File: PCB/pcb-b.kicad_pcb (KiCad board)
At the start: 2 copper layers, 116.9 x 83.4 mm, 104 parts, among them IC2 BDX34C, IC3 BDX34C, K1 RT42xxxx, Q1 D45VH10, Q10 BC337, Q11 BC337, Q12 BC327, Q13 BC337, Q14 D45VH10, Q15 D45VH10, Q16 BC337, Q17 BC337, Q18 BC327, Q19 BC327, Q2 D45VH10, Q20 BC327, Q3 BC337, Q4 BC337, Q5 BC337, Q6 BC337, Q7 BC337, Q8 BC337, Q9 BC337, U1 L7805, U2 L7805, U3 L7805, U4 ATmega16L-8P

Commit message: fixes
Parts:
- removed Bike_stand1, Decomp_1, LightOnOff_sw1, addLights1, powerOFF1: Conn_01x02, Connector_PinSocket_2.54mm:PinSocket_1x02_P2.54mm_Vertical
- removed C2: 100nF, Capacitor_THT:C_Disc_D4.3mm_W1.9mm_P5.00mm
- removed D3, D4: 2V, Diode_THT:D_DO-35_SOD27_P7.62mm_Horizontal
- removed KeyLocker1, RearDevs1: Conn_01x08, Connector_PinHeader_2.54mm:PinHeader_1x08_P2.54mm_Vertical
- removed Q19, Q20: BC327, Package_TO_SOT_THT:TO-92L_Inline_Wide
- removed R1: 1K, Resistor_THT:R_Axial_DIN0207_L6.3mm_D2.5mm_P10.16mm_Horizontal
- removed RA45: 10K, Resistor_THT:R_Axial_DIN0207_L6.3mm_D2.5mm_P7.62mm_Horizontal
- removed RA46, RA47: 3K, Resistor_THT:R_Axial_DIN0207_L6.3mm_D2.5mm_P7.62mm_Horizontal
- removed RA48, RA49: 100K, Resistor_THT:R_Axial_DIN0207_L6.3mm_D2.5mm_P7.62mm_Horizontal
- removed RS232-1: Conn_01x03, Connector_Hirose:Hirose_DF63M-3P-3.96DSA_1x03_P3.96mm_Vertical
- removed RV1, RV2: 10K, Potentiometer_THT:Potentiometer_Bourns_3296W_Vertical
- removed U4: ATmega16L-8P, Package_DIP:DIP-40_W15.24mm
- removed leftCtrls-faston1: Conn_01x01, Connector_Wire:SolderWire-0.75sqmm_1x01_D1.25mm_OD2.3mm
- removed leftCtrls_conn1, rightCtrls_conn1: Conn_01x06, Connector_PinHeader_2.54mm:PinHeader_1x06_P2.54mm_Vertical
- added to_pcA2: Conn_01x05, Connector_PinSocket_2.54mm:PinSocket_1x05_P2.54mm_Vertical, F.Cu at (135.1, 112.2)
- added to_pcA3: Conn_01x05, Connector_PinSocket_2.54mm:PinSocket_1x05_P2.54mm_Vertical, F.Cu at (182.8, 112.2)
- added to_pcbA1: Conn_01x06, Connector_PinSocket_2.54mm:PinSocket_1x06_P2.54mm_Vertical, F.Cu at (135.2, 86.7)
- added to_pcbA4: Conn_01x06, Connector_PinSocket_2.54mm:PinSocket_1x06_P2.54mm_Vertical, F.Cu at (182.6, 86.8)
- Q12: value BC327 -> BC337
- Q16, Q17: value BC337 -> BC327
- RA15: footprint Resistor_THT:R_Axial_DIN0207_L6.3mm_D2.5mm_P7.62mm_Horizontal -> Resistor_THT:R_Axial_DIN0414_L11.9mm_D4.5mm_P15.24mm_Horizontal
- RA23: value 5K -> 100K
- RA29: value 10K -> 1K
- RA31: value 100K -> 3K
- RA33: value 10K -> 3K
- RA41: value 4K -> 100K
- RA43, RA44: value 100K -> 10K
- RA7: value 1K -> 5K
- RA8: value 4K -> 10K
- moved K1 105.5 mm to (103.4, 135.2), turned to 0 degrees
- moved RA15 103.0 mm to (214.1, 65.9)
- moved RA42 89.9 mm to (187.0, 79.9)
- moved koso-1 77.3 mm to (202.7, 60.3), turned to 90 degrees
- moved RA29 59.3 mm to (140.7, 82.9), turned to 0 degrees
- moved Q12 58.3 mm to (142.5, 80.2), turned to 90 degrees
- moved Q16 57.2 mm to (152.7, 87.5), turned to 0 degrees
- moved Q18 53.6 mm to (177.5, 74.3), turned to 0 degrees
- moved RA7 52.2 mm to (141.0, 72.3), turned to 0 degrees
- moved RA30 51.2 mm to (165.6, 79.6)
- moved Q13 47.9 mm to (163.1, 76.1)
- moved RA31 46.8 mm to (173.2, 76.1), turned to 180 degrees
- moved Q9 46.0 mm to (136.7, 73.3), turned to -90 degrees
- moved USB-5V1 45.9 mm to (145.8, 136.5)
- moved RA34 44.8 mm to (125.2, 73.3), turned to 180 degrees
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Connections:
- K1 pad A2: +12V -> tempPower
- Q11 pad 1: Net-(Q11-Pad1) -> Net-(K1-PadA1)
- Q11 pad 2: Net-(D4-Pad2) -> Net-(Q11-Pad2)
- Q12 pad 1: tempPower -> Net-(Q12-Pad1)
- Q12 pad 2: Net-(Q12-Pad2) -> i_powerOFF
- Q12 pad 3: +5V -> GND
- Q13 pad 1: Net-(K1-PadA1) -> Net-(Q13-Pad1)
- Q13 pad 2: Net-(D3-Pad2) -> Net-(Q13-Pad2)
- Q16 pad 1: Net-(Q16-Pad1) -> tempPower
- Q16 pad 3: GND -> +5V
- Q17 pad 1: Net-(D3-Pad1) -> Net-(Q17-Pad1)
- Q17 pad 3: GND -> +12V
- Q18 pad 1: GND -> Net-(Q17-Pad1)
- Q18 pad 3: Net-(D4-Pad1) -> +12V
- RA23 pad 1: Net-(Q9-Pad2) -> Net-(Q16-Pad2)
- RA23 pad 2: o_horn -> +5V
- RA29 pad 1: Net-(Q18-Pad2) -> Net-(Q12-Pad1)
- RA29 pad 2: i_powerOFF -> Net-(Q16-Pad2)
- RA30 pad 1: Net-(D4-Pad2) -> Net-(Q13-Pad1)
- RA30 pad 2: GND -> +12V
- RA31 pad 1: Net-(D3-Pad2) -> Net-(Q17-Pad2)
- RA31 pad 2: GND -> Net-(Q13-Pad1)
- RA33 pad 1: Net-(Q17-Pad2) -> Net-(Q18-Pad2)
- RA33 pad 2: o_engineOFF -> Net-(Q13-Pad1)
- RA41 pad 1: Net-(D3-Pad1) -> i_powerOFF
- RA41 pad 2: o_keepAlive -> GND
- RA43 pad 1: GND -> i_powerOFF
- RA43 pad 2: Net-(Q17-Pad2) -> o_keepAlive
- RA44 pad 1: +5V -> Net-(Q11-Pad2)
- RA44 pad 2: Net-(Q18-Pad2) -> o_engineON
- RA7 pad 1: Net-(Q11-Pad1) -> Net-(Q9-Pad2)
- RA7 pad 2: Net-(Q12-Pad2) -> o_horn
- RA8 pad 1: Net-(D4-Pad1) -> i_powerOFF
- RA8 pad 2: o_keepAlive -> Net-(Q13-Pad2)
- koso-1 pad 2: Net-(Q19-Pad1) -> Net-(Q17-Pad1)
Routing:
- net +5V: track 328.6 -> 122.0 mm, vias 1 -> 0
- net GND: track 478.3 -> 332.3 mm, vias 0 -> 2
- net Net-(Q15-Pad1): track 163.5 -> 34.3 mm, vias 2 -> 0
- net Net-(Q9-Pad1): track 5.44 -> 116.9 mm, vias 0 -> 1
- net Net-(U4-Pad15): track 78.8 -> 0.00 mm, vias 1 -> 0
- net i_bykeStand: track 70.3 -> 0.00 mm
- net tempPower: track 156.0 -> 85.8 mm, vias 0 -> 2
- net Net-(K1-PadA1): track 100.7 -> 30.9 mm
- net c_rightArrow: track 153.8 -> 85.2 mm, vias 2 -> 1
- net i_neutral: track 68.3 -> 0.00 mm
- net Net-(RS232-1-Pad2): track 64.1 -> 0.00 mm, vias 1 -> 0
- net i_horn: track 62.3 -> 0.00 mm
- net i_rightArrow: track 61.0 -> 0.00 mm
- net i_upLight: track 59.6 -> 0.00 mm
- net i_leftArrow: track 59.0 -> 0.00 mm
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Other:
- outline, holes or cut-outs redrawn

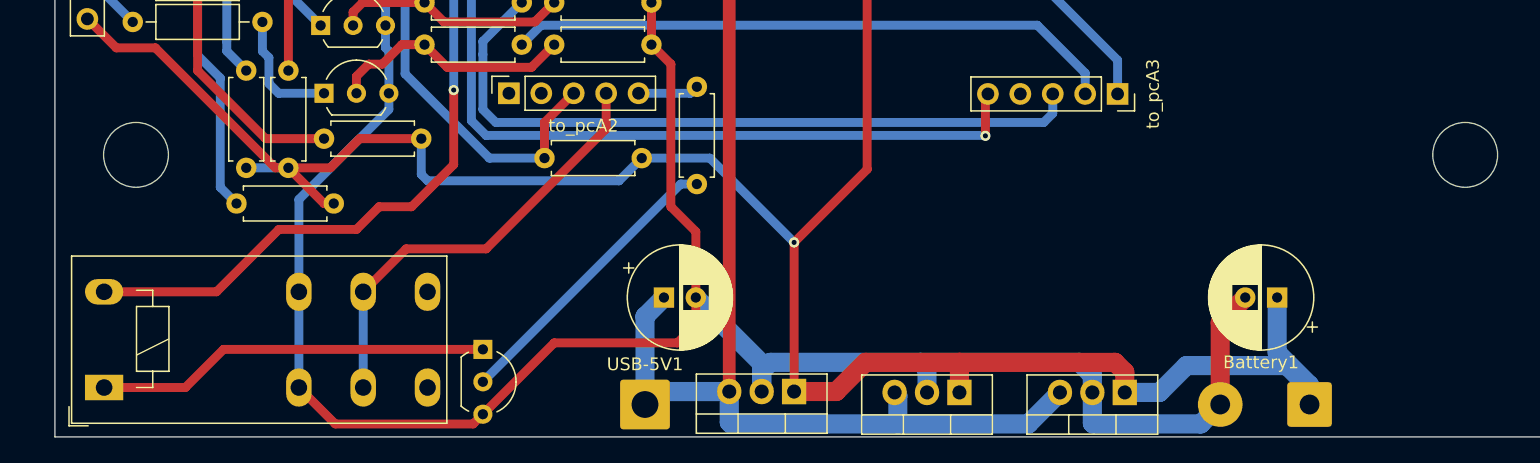
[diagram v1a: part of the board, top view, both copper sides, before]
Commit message: Wrong relay's footprint fixed
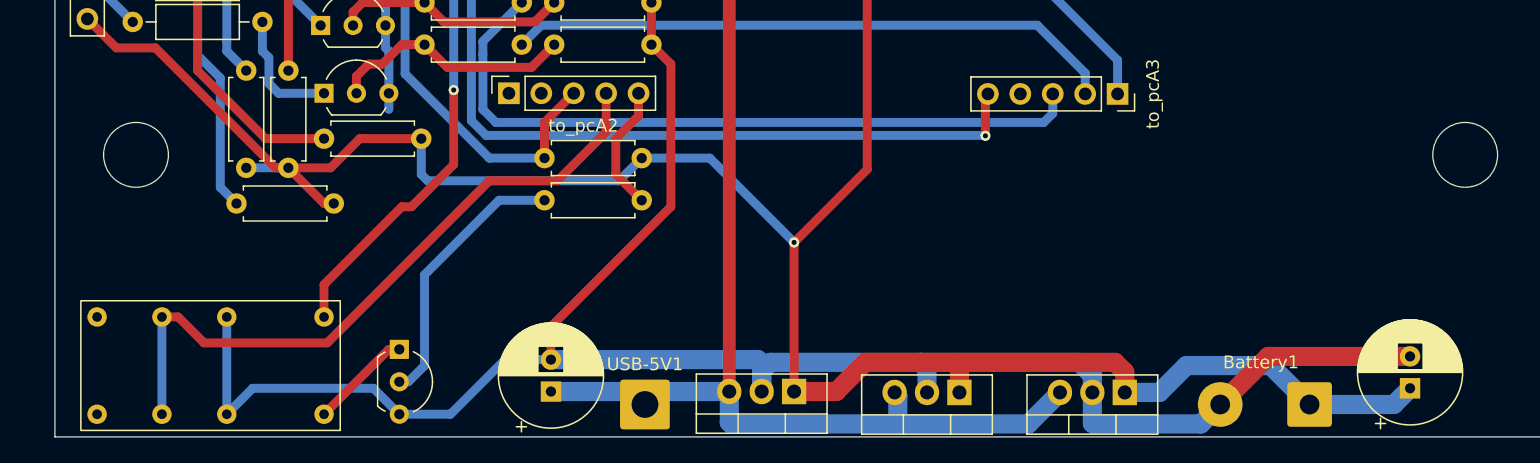
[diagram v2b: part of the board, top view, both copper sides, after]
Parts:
- removed K1: RT42xxxx, Relay_THT:Relay_DPDT_Schrack-RT2-FormC_RM5mm
- added U4: HK19F-DC12-SHG, HK19F:HK19F-DC12-SHG, F.Cu at (113.0, 127.1)
- moved C9 12.6 mm to (205.7, 135.3), turned to 90 degrees
- moved RA44 12.0 mm to (137.9, 120.5), turned to 0 degrees
- moved C1 11.5 mm to (138.4, 135.5), turned to 90 degrees
- moved Q11 6.55 mm to (126.6, 132.2)
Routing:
- net Net-(Q11-Pad1): track 30.9 -> 8.00 mm
- net c_engineOFF: track 34.6 -> 53.1 mm
- net tempPower: track 85.8 -> 70.8 mm
- net o_engineON: track 4.78 -> 9.96 mm
- net +12V: track 246.2 -> 244.4 mm
- net Net-(Q11-Pad2): track 23.2 -> 21.4 mm
- net GND: track 332.3 -> 331.0 mm
- net +5V: track 122.0 -> 120.8 mm

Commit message: small errors and warnings fixed. Ready to be printed
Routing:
- net GND: track 331.0 -> 361.1 mm
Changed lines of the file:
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@@
     (property "Sheetname" "")
     (attr exclude_from_pos_files)
-    (fp_text reference "USB-5V1" (at 0 -3.15) (layer "F.SilkS")
+    (fp_text reference "USB-5V1" (at 0.762 -3.302) (layer "F.SilkS")
       (effects (font (size 1 1) (thickness 0.15)))
     )
@@
   )
   (gr_rect (start 133.46 88.559) (end 184.514 110.403) (layer "B.Mask") (width 0.12) (fill none))
-  (gr_rect (start 99.576 72.786) (end 216.416 123.078) (layer "F.Mask") (width 0.1) (fill none))
   (gr_rect (start 171.712 55.585) (end 173.998 60.665) (layer "F.Mask") (width 0.1) (fill solid))
   (gr_rect (start 132.342 55.585) (end 134.628 60.665) (layer "F.Mask") (width 0.1) (fill solid))
@@
   (segment (start 137.676 96.662) (end 175.522 96.662) (width 0.7) (layer "B.Cu") (net 39))
   (segment (start 136.152 95.138) (end 137.676 96.662) (width 0.7) (layer "B.Cu") (net 39))
+  (segment (start 129.802 89.296) (end 129.802 86.756) (width 0.7) (layer "F.Cu") (net 40))
+  (segment (start 129.802 86.756) (end 136.718 79.84) (width 0.7) (layer "F.Cu") (net 40))
   (segment (start 154.44 71.516) (end 152.9 69.976) (width 0.7) (layer "F.Cu") (net 40))
   (segment (start 190.874 136.54) (end 194.644 132.77) (width 1.5) (layer "F.Cu") (net 40))
@@
   (segment (start 157.996 71.262) (end 157.996 76.088) (width 0.7) (layer "F.Cu") (net 40))
   (segment (start 142.502 73.294) (end 142.502 75.072) (width 0.7) (layer "F.Cu") (net 40))
+  (segment (start 130.564 90.058) (end 129.802 89.296) (width 0.7) (layer "F.Cu") (net 40))
+  (segment (start 144.534 90.058) (end 130.564 90.058) (width 0.7) (layer "F.Cu") (net 40))
+  (segment (start 146.312 91.836) (end 144.534 90.058) (width 0.7) (layer "F.Cu") (net 40))
   (segment (start 126.442 78.364) (end 133.602 78.364) (width 0.7) (layer "F.Cu") (net 40))
   (segment (start 152.9 69.976) (end 145.82 69.976) (width 0.7) (layer "F.Cu") (net 40))
@@
   (segment (start 133.358 76.596) (end 133.358 78.12) (width 0.7) (layer "F.Cu") (net 40))
   (segment (start 147.836 109.87) (end 147.836 121.046) (width 0.7) (layer "F.Cu") (net 40))
+  (segment (start 136.718 79.84) (end 136.718 78.364) (width 0.7) (layer "F.Cu") (net 40))
   (segment (start 133.602 78.364) (end 136.718 78.364) (width 0.7) (layer "F.Cu") (net 40))
   (segment (start 145.82 69.976) (end 142.502 73.294) (width 0.7) (layer "F.Cu") (net 40))
@@
   (segment (start 199.398 60.34) (end 196.884 62.854) (width 0.7) (layer "B.Cu") (net 40))
   (segment (start 167.394 133.238) (end 179.84 133.238) (width 1.5) (layer "B.Cu") (net 40))
-  (segment (start 125.738 113.426) (end 125.738 112.156) (width 0.7) (layer "B.Cu") (net 40))
   (segment (start 154.948 133.317302) (end 154.654698 133.024) (width 1.5) (layer "B.Cu") (net 40))
   (segment (start 125.474 79.332) (end 125.474 84.92) (width 0.7) (layer "B.Cu") (net 40))

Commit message: fixes
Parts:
- added GND-1: ~, Connector_Wire:SolderWire-1.5sqmm_1x03_P6mm_D1.7mm_OD3mm, F.Cu at (197.3, 131.4)
- added GND-2: ~, Connector_Wire:SolderWire-1.5sqmm_1x03_P6mm_D1.7mm_OD3mm, F.Cu at (197.3, 136.5)
- moved C9 26.5 mm to (180.3, 127.7), turned to 0 degrees
- moved Battery1 11.0 mm to (189.5, 129.4), turned to -90 degrees
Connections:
- to_pcA2 pad 1: unconnected-(to_pcA2-Pad1) -> c_RS232_RXD
- to_pcA2 pad 2: unconnected-(to_pcA2-Pad2) -> c_RS232_TXT
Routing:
- net GND: track 361.1 -> 402.7 mm
- net +12V: track 244.4 -> 233.7 mm

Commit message: Merged files
These files have been merged by remotes/origin/ATmega16__dualPCB__bluetoothCockpit branch
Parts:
- removed IC2, IC3: BDX34C, BDX34C:TO270P460X1020X2008-3P
- removed Q11, Q13: BC337, Package_TO_SOT_THT:TO-92L_Inline_Wide
- removed Q16: BC327, Package_TO_SOT_THT:TO-92L_Inline_Wide
- removed RA23: 100K, Resistor_THT:R_Axial_DIN0207_L6.3mm_D2.5mm_P7.62mm_Horizontal
- removed RA29: 1K, Resistor_THT:R_Axial_DIN0207_L6.3mm_D2.5mm_P7.62mm_Horizontal
- added Q19: BC817, Package_TO_SOT_SMD:SOT-23, F.Cu at (123.4, 100.5)
- added Q20: BC817, Package_TO_SOT_SMD:SOT-23, F.Cu at (123.4, 104.1)
- added Q21: BC817, Package_TO_SOT_SMD:SOT-23, F.Cu at (123.4, 107.8)
- Q1, Q14, Q15, Q2: value D45VH10 -> BC817; footprint Package_TO_SOT_THT:TO-220-3_Vertical -> Package_TO_SOT_SMD:SOT-23
- Q10, Q12, Q3: value BC337 -> BC817; footprint Package_TO_SOT_THT:TO-92L_Inline_Wide -> Package_TO_SOT_SMD:SOT-23
- Q4, Q5, Q6, Q7, Q8, Q9: value BC337 -> IRF4905; footprint Package_TO_SOT_THT:TO-92L_Inline_Wide -> Package_TO_SOT_THT:TO-220-3_Vertical
- RA1, RA2, RA3, RA4, RA5, RA6, RA9: footprint Resistor_THT:R_Axial_DIN0207_L6.3mm_D2.5mm_P10.16mm_Horizontal -> Resistor_SMD:R_1206_3216Metric
- RA10, RA11, RA12: footprint Resistor_THT:R_Axial_DIN0414_L11.9mm_D4.5mm_P15.24mm_Horizontal -> Resistor_SMD:R_1206_3216Metric
- RA13, RA14, RA16, RA17, RA18, RA19, RA20, RA21, RA22, RA24, RA25, RA26, RA27, RA28, RA30, RA31, RA32, RA33, RA34, RA35, RA36, RA37, RA38, RA39, RA40, RA41, RA43, RA44, RA7, RA8: footprint Resistor_THT:R_Axial_DIN0207_L6.3mm_D2.5mm_P7.62mm_Horizontal -> Resistor_SMD:R_1206_3216Metric
- RA15: value 240 -> 8K; footprint Resistor_THT:R_Axial_DIN0414_L11.9mm_D4.5mm_P15.24mm_Horizontal -> Resistor_SMD:R_1206_3216Metric
- RA42: value 100K -> 8K; footprint Resistor_THT:R_Axial_DIN0207_L6.3mm_D2.5mm_P7.62mm_Horizontal -> Resistor_SMD:R_1206_3216Metric
- moved Q15 76.8 mm to (123.5, 96.9), turned to 180 degrees
- moved Q10 71.9 mm to (187.2, 85.2)
- moved GND-2 65.2 mm to (133.3, 124.0), turned to 180 degrees
- moved Q3 61.5 mm to (180.4, 92.8), turned to 90 degrees
- moved Q7 56.4 mm to (168.7, 72.2)
- moved Q8 49.5 mm to (155.8, 72.2)
- moved U4 49.2 mm to (157.7, 106.3), turned to 0 degrees
- moved RA15 47.6 mm to (175.0, 93.1), turned to 90 degrees
- moved Q9 45.0 mm to (181.7, 72.2), turned to 0 degrees
- moved Q14 43.5 mm to (123.5, 93.3), turned to 180 degrees
- moved RA8 42.4 mm to (193.0, 84.5), turned to 180 degrees
- moved RA41 39.4 mm to (193.0, 87.0)
- moved RA7 36.8 mm to (172.6, 91.0), turned to 90 degrees
- moved RA43 35.5 mm to (193.1, 89.3), turned to 180 degrees
- moved RA32 34.9 mm to (177.4, 93.2), turned to -90 degrees
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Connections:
- Q1 pad 1: Net-(Q1-Pad1) -> Net-(Q1-B)
- Q1 pad 2: Net-(addLight_p1-Pin_1) -> GND
- Q1 pad 3: Net-(addLight_p1-Pin_2) -> Net-(Q1-C)
- Q10 pad 1: Net-(Q10-C) -> Net-(Q10-B)
- Q10 pad 2: Net-(Q10-B) -> GND
- Q10 pad 3: GND -> Net-(Q10-C)
- Q12 pad 1: Net-(Q12-C) -> Net-(Q12-B)
- Q12 pad 2: i_powerOFF -> GND
- Q12 pad 3: GND -> Net-(Q12-C)
- Q14 pad 1: Net-(Q14-Pad1) -> Net-(Q14-B)
- Q14 pad 2: Net-(DownLight_p1-Pin_1) -> GND
- Q14 pad 3: Net-(DownLight_p1-Pin_2) -> Net-(Q14-C)
- Q15 pad 1: Net-(Q15-Pad1) -> Net-(Q15-B)
- Q15 pad 2: Net-(Horn_p1-Pin_1) -> GND
- Q15 pad 3: Net-(Horn_p1-Pin_2) -> c_leftArrow
- Q2 pad 1: Net-(Q2-Pad1) -> Net-(Q2-B)
- Q2 pad 2: Net-(UpLight_p1-Pin_1) -> GND
- Q2 pad 3: Net-(UpLight_p1-Pin_2) -> Net-(Q2-C)
- Q3 pad 1: Net-(Q3-C) -> Net-(Q3-B)
- Q3 pad 2: Net-(Q3-B) -> GND
- Q3 pad 3: GND -> Net-(Q3-C)
- Q4 pad 1: Net-(Q4-C) -> Net-(Q4-G)
- Q4 pad 2: Net-(Q4-B) -> Net-(Q4-D)
- Q4 pad 3: GND -> Net-(Q4-S)
- Q5 pad 1: Net-(Q5-C) -> Net-(Q5-G)
- Q5 pad 2: Net-(Q5-B) -> Net-(Q5-D)
- Q5 pad 3: GND -> Net-(Q5-S)
- Q6 pad 1: c_leftArrow -> Net-(Q6-G)
- Q6 pad 2: Net-(Q6-B) -> Net-(DownLight_p1-Pin_2)
- Q6 pad 3: GND -> Net-(DownLight_p1-Pin_1)
- Q7 pad 1: c_rightArrow -> Net-(Q7-G)
- Q7 pad 2: Net-(Q7-B) -> Net-(Arrow_p1-Pin_1)
- Q7 pad 3: GND -> Net-(Arrow_p1-Pin_2)
- Q8 pad 1: Net-(Q8-C) -> Net-(Q8-G)
- Q8 pad 2: Net-(Q8-B) -> Net-(Arrow_p1-Pin_3)
- Q8 pad 3: GND -> Net-(Arrow_p1-Pin_2)
- Q9 pad 1: Net-(Q9-C) -> Net-(Q9-G)
- Q9 pad 2: Net-(Q9-B) -> Net-(Horn_p1-Pin_2)
- Q9 pad 3: GND -> Net-(Horn_p1-Pin_1)
- RA1 pad 1: Net-(Q3-C) -> Net-(Q1-C)
- RA10 pad 1: Net-(Q3-C) -> Net-(Q1-C)
- RA10 pad 2: Net-(Q1-Pad1) -> Net-(Q4-G)
- RA11 pad 1: Net-(Q4-C) -> Net-(Q2-C)
- RA11 pad 2: Net-(Q2-Pad1) -> Net-(Q5-G)
- RA12 pad 1: Net-(Q5-C) -> Net-(Q14-C)
- RA12 pad 2: Net-(Q14-Pad1) -> Net-(Q6-G)
- RA13 pad 2: Net-(IC2-B) -> Net-(Q7-G)
- RA14 pad 2: Net-(IC3-B) -> Net-(Q8-G)
- RA15 pad 1: Net-(Q9-C) -> Net-(Q9-G)
- RA15 pad 2: Net-(Q15-Pad1) -> Net-(Q3-C)
- RA16 pad 1: Net-(Q10-B) -> Net-(Q21-B)
- RA17 pad 1: Net-(Q8-B) -> Net-(Q20-B)
- RA18 pad 1: Net-(Q7-B) -> Net-(Q19-B)
- RA19 pad 1: Net-(Q6-B) -> Net-(Q15-B)
- RA2 pad 1: Net-(Q4-C) -> Net-(Q2-C)
- RA20 pad 1: Net-(Q5-B) -> Net-(Q14-B)
- RA21 pad 1: Net-(Q4-B) -> Net-(Q2-B)
- RA22 pad 1: Net-(Q3-B) -> Net-(Q1-B)
- RA24 pad 2: Net-(Q3-C) -> Net-(Q4-G)
- RA25 pad 2: Net-(Q4-C) -> Net-(Q5-G)
- RA26 pad 2: Net-(Q5-C) -> Net-(Q6-G)
- RA27 pad 2: c_leftArrow -> Net-(Q7-G)
- RA28 pad 2: c_rightArrow -> Net-(Q8-G)
- RA3 pad 1: Net-(Q5-C) -> Net-(Q14-C)
- RA30 pad 1: Net-(Q13-C) -> Net-(Q10-C)
- RA31 pad 2: Net-(Q13-C) -> Net-(Q10-C)
- RA32 pad 1: Net-(Q9-B) -> Net-(Q3-B)
- RA33 pad 2: Net-(Q13-C) -> Net-(Q10-C)
- RA34 pad 1: Net-(Q3-B) -> Net-(Q1-B)
- RA35 pad 1: Net-(Q4-B) -> Net-(Q2-B)
- RA36 pad 1: Net-(Q5-B) -> Net-(Q14-B)
- RA37 pad 1: Net-(Q6-B) -> Net-(Q15-B)
- RA38 pad 1: Net-(Q7-B) -> Net-(Q19-B)
- RA39 pad 1: Net-(Q8-B) -> Net-(Q20-B)
- RA40 pad 1: Net-(Q10-B) -> Net-(Q21-B)
- RA42 pad 1: +12V -> Net-(Q9-G)
- RA42 pad 2: Net-(Q15-Pad1) -> +12V
- RA44 pad 1: Net-(Q11-B) -> Net-(Q12-B)
- RA6 pad 1: Net-(Q8-C) -> Net-(Q20-C)
- RA7 pad 1: Net-(Q9-B) -> Net-(Q3-B)
- RA8 pad 2: Net-(Q13-B) -> Net-(Q10-B)
- RA9 pad 1: Net-(Q10-C) -> Net-(Q21-C)
- U4 pad 8: Net-(Q11-C) -> Net-(Q12-C)
- UpLight_p1 pad 1: Net-(UpLight_p1-Pin_1) -> Net-(Q5-S)
- UpLight_p1 pad 2: Net-(UpLight_p1-Pin_2) -> Net-(Q5-D)
- addLight_p1 pad 1: Net-(addLight_p1-Pin_1) -> Net-(Q4-S)
- addLight_p1 pad 2: Net-(addLight_p1-Pin_2) -> Net-(Q4-D)
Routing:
- net Net-(Q9-C): track 116.9 -> 0.00 mm, vias 1 -> 0
- net Net-(Q3-C): track 114.3 -> 7.45 mm
- net Net-(Q7-G): track 0.00 -> 78.7 mm, vias 0 -> 3
- net Net-(Q8-G): track 0.00 -> 66.5 mm, vias 0 -> 3
- net Net-(Q4-C): track 61.7 -> 0.00 mm, vias 1 -> 0
- net c_leftArrow: track 145.4 -> 87.4 mm, vias 1 -> 3
- net Net-(Q9-G): track 0.00 -> 57.1 mm, vias 0 -> 1
- net Net-(Q6-G): track 0.00 -> 57.0 mm, vias 0 -> 2
- net Net-(IC2-B): track 55.0 -> 0.00 mm
- net Net-(Q5-C): track 54.2 -> 0.00 mm
- net Net-(Q5-G): track 0.00 -> 47.7 mm, vias 0 -> 2
- net GND: track 402.7 -> 360.4 mm, vias 2 -> 17
- net Net-(IC3-B): track 40.6 -> 0.00 mm
- net Net-(Q4-G): track 0.00 -> 40.4 mm, vias 0 -> 2
- net Net-(Q14-Pad1): track 39.6 -> 0.00 mm
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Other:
- board size 116.9 x 83.4 mm -> 117.6 x 58.2 mm
